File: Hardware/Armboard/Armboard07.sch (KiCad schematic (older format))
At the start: 30 parts

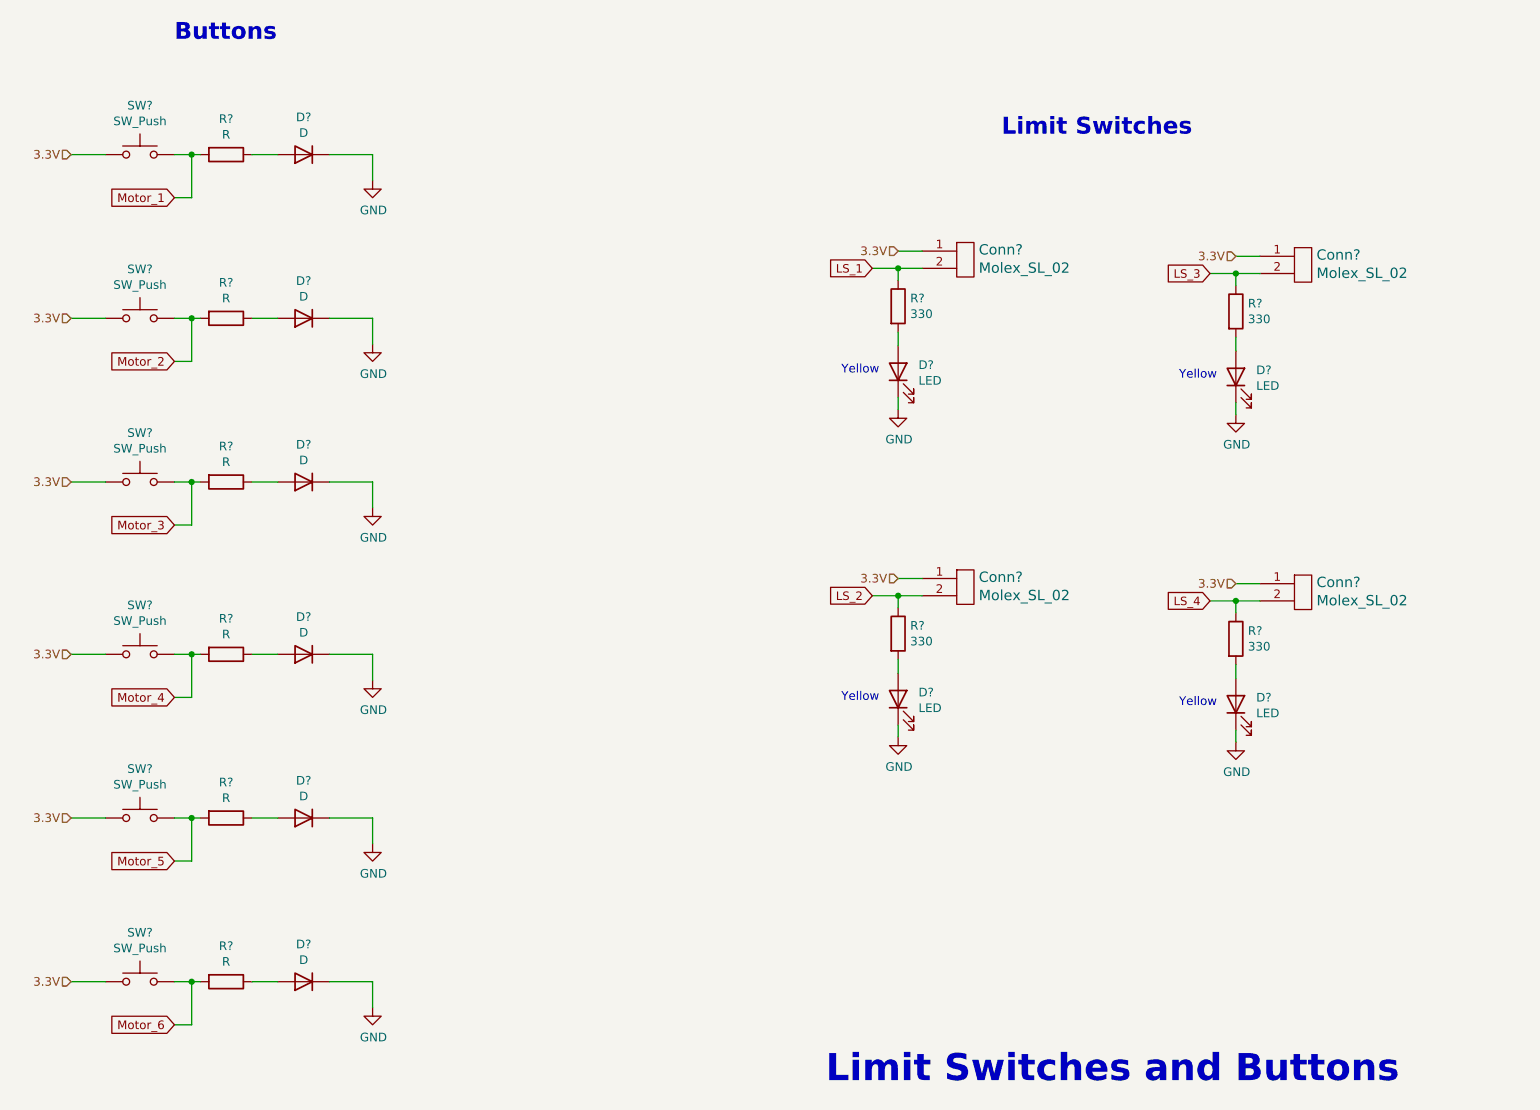
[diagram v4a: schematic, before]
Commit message: Fixed buttons/switches page, changed resistor values, fixed some tiva connections
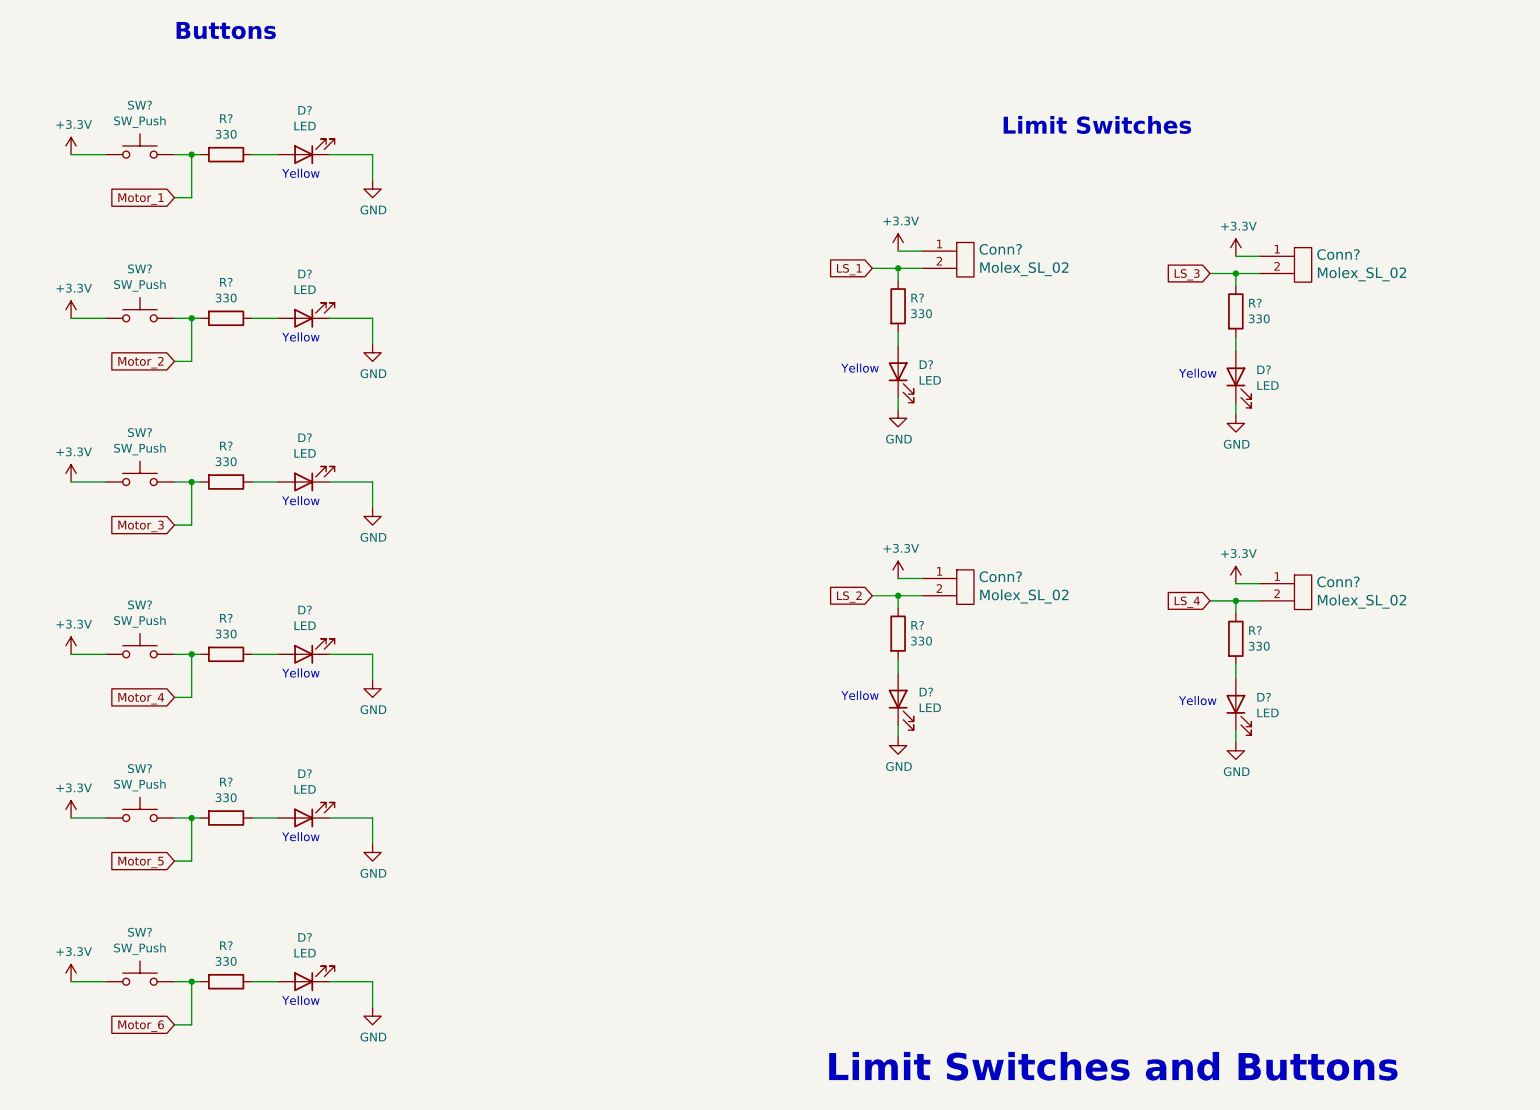
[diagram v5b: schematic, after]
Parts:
- removed D? (x6): D, symbol Device:D
- added D? (x6): LED, symbol Device:LED
- R? (x6): value R -> 330
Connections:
- net GND: now also D?.1 (K), D?.1 (K), D?.1 (K), D?.1 (K), D?.1 (K), D?.1 (K)
- net at R?.1: now also D?.2 (A) (x6)
- net 3.3V renamed +3V3
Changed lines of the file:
@@
 P 3050 1750
 F 0 "R?" V 2843 1750 50  0000 C CNN
-F 1 "R" V 2934 1750 50  0000 C CNN
+F 1 "330" V 2934 1750 50  0000 C CNN
 F 2 "" V 2980 1750 50  0001 C CNN
 F 3 "~" H 3050 1750 50  0001 C CNN
@@
 Wire Wire Line
 	2850 1750 2900 1750
-$Comp
-L Device:D D?
-U 1 1 5F86348C
-P 3500 1750
-F 0 "D?" H 3500 1533 50  0000 C CNN
-F 1 "D" H 3500 1624 50  0000 C CNN
-F 2 "" H 3500 1750 50  0001 C CNN
-F 3 "~" H 3500 1750 50  0001 C CNN
-	1    3500 1750
-	-1   0    0    1
-$EndComp
 $Comp
 L power:GND #PWR?
@@
 P 3050 2700
 F 0 "R?" V 2843 2700 50  0000 C CNN
-F 1 "R" V 2934 2700 50  0000 C CNN
+F 1 "330" V 2934 2700 50  0000 C CNN
 F 2 "" V 2980 2700 50  0001 C CNN
 F 3 "~" H 3050 2700 50  0001 C CNN
@@
 Wire Wire Line
 	2850 2700 2900 2700
-$Comp
-L Device:D D?
-U 1 1 5F86509F
-P 3500 2700
-F 0 "D?" H 3500 2483 50  0000 C CNN
-F 1 "D" H 3500 2574 50  0000 C CNN
-F 2 "" H 3500 2700 50  0001 C CNN
-F 3 "~" H 3500 2700 50  0001 C CNN
-	1    3500 2700
-	-1   0    0    1
-$EndComp
 $Comp
 L power:GND #PWR?
@@
 P 3050 3650
 F 0 "R?" V 2843 3650 50  0000 C CNN
-F 1 "R" V 2934 3650 50  0000 C CNN
+F 1 "330" V 2934 3650 50  0000 C CNN
 F 2 "" V 2980 3650 50  0001 C CNN
 F 3 "~" H 3050 3650 50  0001 C CNN
@@
 Wire Wire Line
 	2850 3650 2900 3650
-$Comp
-L Device:D D?
-U 1 1 5F866115
-P 3500 3650
-F 0 "D?" H 3500 3433 50  0000 C CNN
-F 1 "D" H 3500 3524 50  0000 C CNN
-F 2 "" H 3500 3650 50  0001 C CNN
-F 3 "~" H 3500 3650 50  0001 C CNN
-	1    3500 3650
-	-1   0    0    1
-$EndComp
 $Comp
 L power:GND #PWR?
@@
 P 3050 4650
 F 0 "R?" V 2843 4650 50  0000 C CNN
-F 1 "R" V 2934 4650 50  0000 C CNN
+F 1 "330" V 2934 4650 50  0000 C CNN
 F 2 "" V 2980 4650 50  0001 C CNN
 F 3 "~" H 3050 4650 50  0001 C CNN
@@
 Wire Wire Line
 	2850 4650 2900 4650
-$Comp
-L Device:D D?
-U 1 1 5F868D0E
-P 3500 4650
-F 0 "D?" H 3500 4433 50  0000 C CNN
-F 1 "D" H 3500 4524 50  0000 C CNN
-F 2 "" H 3500 4650 50  0001 C CNN
-F 3 "~" H 3500 4650 50  0001 C CNN
-	1    3500 4650
-	-1   0    0    1
-$EndComp
 $Comp
 L power:GND #PWR?
@@
 P 3050 5600
 F 0 "R?" V 2843 5600 50  0000 C CNN
-F 1 "R" V 2934 5600 50  0000 C CNN
+F 1 "330" V 2934 5600 50  0000 C CNN
 F 2 "" V 2980 5600 50  0001 C CNN
 F 3 "~" H 3050 5600 50  0001 C CNN
@@
 Wire Wire Line
 	2850 5600 2900 5600
-$Comp
-L Device:D D?
-U 1 1 5F868D37
-P 3500 5600
-F 0 "D?" H 3500 5383 50  0000 C CNN
-F 1 "D" H 3500 5474 50  0000 C CNN
-F 2 "" H 3500 5600 50  0001 C CNN
-F 3 "~" H 3500 5600 50  0001 C CNN
-	1    3500 5600
-	-1   0    0    1
-$EndComp
 $Comp
 L power:GND #PWR?
@@
 P 3050 6550
 F 0 "R?" V 2843 6550 50  0000 C CNN
-F 1 "R" V 2934 6550 50  0000 C CNN
+F 1 "330" V 2934 6550 50  0000 C CNN
 F 2 "" V 2980 6550 50  0001 C CNN
 F 3 "~" H 3050 6550 50  0001 C CNN
@@
 Wire Wire Line
 	2850 6550 2900 6550
-$Comp
-L Device:D D?
-U 1 1 5F868D60
-P 3500 6550
-F 0 "D?" H 3500 6333 50  0000 C CNN
-F 1 "D" H 3500 6424 50  0000 C CNN
-F 2 "" H 3500 6550 50  0001 C CNN
-F 3 "~" H 3500 6550 50  0001 C CNN
-	1    3500 6550
-	-1   0    0    1
-$EndComp
 Text Notes 7550 1650 0    98   ~ 20
 Limit Switches
 Text Notes 2750 1100 0    98   ~ 20
 Buttons
-Text HLabel 2150 1750 0    50   Input ~ 0
-3.3V
-Text HLabel 2150 2700 0    50   Input ~ 0
-3.3V
-Text HLabel 2150 3650 0    50   Input ~ 0
-3.3V
-Text HLabel 2150 4650 0    50   Input ~ 0
-3.3V
-Text HLabel 2150 5600 0    50   Input ~ 0
-3.3V
-Text HLabel 2150 6550 0    50   Input ~ 0
-3.3V
-Text HLabel 6950 4210 0    50   Input ~ 0
-3.3V
-Text HLabel 8910 4240 0    50   Input ~ 0
-3.3V
-Text HLabel 8910 2340 0    50   Input ~ 0
-3.3V
-Text HLabel 6950 2310 0    50   Input ~ 0
-3.3V
+$Comp
+L power:+3.3V #PWR?
+U 1 1 5F91F195
+P 2150 1750
+F 0 "#PWR?" H 2150 1600 50  0001 C CNN
+F 1 "+3.3V" H 2165 1923 50  0000 C CNN
+F 2 "" H 2150 1750 50  0001 C CNN
+F 3 "" H 2150 1750 50  0001 C CNN
+	1    2150 1750
+	1    0    0    -1
+$EndComp
+$Comp
+L power:+3.3V #PWR?
+U 1 1 5F923263
+P 2150 2700
+F 0 "#PWR?" H 2150 2550 50  0001 C CNN
+F 1 "+3.3V" H 2165 2873 50  0000 C CNN
+F 2 "" H 2150 2700 50  0001 C CNN
+F 3 "" H 2150 2700 50  0001 C CNN
+	1    2150 2700
+	1    0    0    -1
+$EndComp
+$Comp
+L power:+3.3V #PWR?
+U 1 1 5F924E57
+P 2150 3650
+F 0 "#PWR?" H 2150 3500 50  0001 C CNN
+F 1 "+3.3V" H 2165 3823 50  0000 C CNN
+F 2 "" H 2150 3650 50  0001 C CNN
+F 3 "" H 2150 3650 50  0001 C CNN
+	1    2150 3650
+	1    0    0    -1
+$EndComp
+$Comp
+L power:+3.3V #PWR?
+U 1 1 5F9269C5
+P 2150 4650
+F 0 "#PWR?" H 2150 4500 50  0001 C CNN
+F 1 "+3.3V" H 2165 4823 50  0000 C CNN
+F 2 "" H 2150 4650 50  0001 C CNN
+F 3 "" H 2150 4650 50  0001 C CNN
+	1    2150 4650
+	1    0    0    -1
+$EndComp
+$Comp
+L power:+3.3V #PWR?
+U 1 1 5F9284DA
+P 2150 5600
+F 0 "#PWR?" H 2150 5450 50  0001 C CNN
+F 1 "+3.3V" H 2165 5773 50  0000 C CNN
+F 2 "" H 2150 5600 50  0001 C CNN
+F 3 "" H 2150 5600 50  0001 C CNN
+	1    2150 5600
+	1    0    0    -1
+$EndComp
+$Comp
+L power:+3.3V #PWR?
+U 1 1 5F92A093
+P 2150 6550
+F 0 "#PWR?" H 2150 6400 50  0001 C CNN
+F 1 "+3.3V" H 2165 6723 50  0000 C CNN
+F 2 "" H 2150 6550 50  0001 C CNN
+F 3 "" H 2150 6550 50  0001 C CNN
+	1    2150 6550
+	1    0    0    -1
+$EndComp
+$Comp
+L power:+3.3V #PWR?
+U 1 1 5F932624
+P 6950 2310
+F 0 "#PWR?" H 6950 2160 50  0001 C CNN
+F 1 "+3.3V" H 6965 2483 50  0000 C CNN
+F 2 "" H 6950 2310 50  0001 C CNN
+F 3 "" H 6950 2310 50  0001 C CNN
+	1    6950 2310
+	1    0    0    -1
+$EndComp
+$Comp
+L power:+3.3V #PWR?
+U 1 1 5F934170
+P 8910 2340
+F 0 "#PWR?" H 8910 2190 50  0001 C CNN
+F 1 "+3.3V" H 8925 2513 50  0000 C CNN
+F 2 "" H 8910 2340 50  0001 C CNN
+F 3 "" H 8910 2340 50  0001 C CNN
+	1    8910 2340
+	1    0    0    -1
+$EndComp
+$Comp
+L power:+3.3V #PWR?
+U 1 1 5F935C61
+P 8910 4240
+F 0 "#PWR?" H 8910 4090 50  0001 C CNN
+F 1 "+3.3V" H 8925 4413 50  0000 C CNN
+F 2 "" H 8910 4240 50  0001 C CNN
+F 3 "" H 8910 4240 50  0001 C CNN
+	1    8910 4240
+	1    0    0    -1
+$EndComp
+$Comp
+L power:+3.3V #PWR?
+U 1 1 5F93ADAC
+P 6950 4210
+F 0 "#PWR?" H 6950 4060 50  0001 C CNN
+F 1 "+3.3V" H 6965 4383 50  0000 C CNN
+F 2 "" H 6950 4210 50  0001 C CNN
+F 3 "" H 6950 4210 50  0001 C CNN
+	1    6950 4210
+	1    0    0    -1
+$EndComp
+$Comp
+L Device:LED D?
+U 1 1 5F93EBEE
+P 3500 1750
+F 0 "D?" H 3493 1495 50  0000 C CNN
+F 1 "LED" H 3493 1586 50  0000 C CNN
+F 2 "" H 3500 1750 50  0001 C CNN
+F 3 "~" H 3500 1750 50  0001 C CNN
+	1    3500 1750
+	-1   0    0    1
+$EndComp
+Text Notes 3375 1900 0    50   ~ 0
+Yellow
+$Comp
+L Device:LED D?
+U 1 1 5F9425FB
+P 3500 2700
+F 0 "D?" H 3493 2445 50  0000 C CNN
+F 1 "LED" H 3493 2536 50  0000 C CNN
+F 2 "" H 3500 2700 50  0001 C CNN
+F 3 "~" H 3500 2700 50  0001 C CNN
+	1    3500 2700
+	-1   0    0    1
+$EndComp
+Text Notes 3375 2850 0    50   ~ 0
+Yellow
+$Comp
+L Device:LED D?
+U 1 1 5F944196
+P 3500 3650
+F 0 "D?" H 3493 3395 50  0000 C CNN
+F 1 "LED" H 3493 3486 50  0000 C CNN
+F 2 "" H 3500 3650 50  0001 C CNN
+F 3 "~" H 3500 3650 50  0001 C CNN
+	1    3500 3650
+	-1   0    0    1
+$EndComp
+Text Notes 3375 3800 0    50   ~ 0
+Yellow
+$Comp
+L Device:LED D?
+U 1 1 5F945DAF
+P 3500 4650
+F 0 "D?" H 3493 4395 50  0000 C CNN
+F 1 "LED" H 3493 4486 50  0000 C CNN
+F 2 "" H 3500 4650 50  0001 C CNN
+F 3 "~" H 3500 4650 50  0001 C CNN
+	1    3500 4650
+	-1   0    0    1
+$EndComp
+Text Notes 3375 4800 0    50   ~ 0
+Yellow
+$Comp
+L Device:LED D?
+U 1 1 5F9479B6
+P 3500 5600
+F 0 "D?" H 3493 5345 50  0000 C CNN
+F 1 "LED" H 3493 5436 50  0000 C CNN
+F 2 "" H 3500 5600 50  0001 C CNN
+F 3 "~" H 3500 5600 50  0001 C CNN
+	1    3500 5600
+	-1   0    0    1
+$EndComp
+Text Notes 3375 5750 0    50   ~ 0
+Yellow
+$Comp
+L Device:LED D?
+U 1 1 5F9495A5
+P 3500 6550
+F 0 "D?" H 3493 6295 50  0000 C CNN
+F 1 "LED" H 3493 6386 50  0000 C CNN
+F 2 "" H 3500 6550 50  0001 C CNN
+F 3 "~" H 3500 6550 50  0001 C CNN
+	1    3500 6550
+	-1   0    0    1
+$EndComp
+Text Notes 3375 6700 0    50   ~ 0
+Yellow
 $EndSCHEMATC
